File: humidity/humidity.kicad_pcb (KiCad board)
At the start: 2 copper layers, 59.7 x 27.9 mm, 19 parts, among them J1 Battery Holder, J2 Conn_01x06, U1 BME280, U2 ESP32-WROOM-32, U3 HT7333-A-SOT89

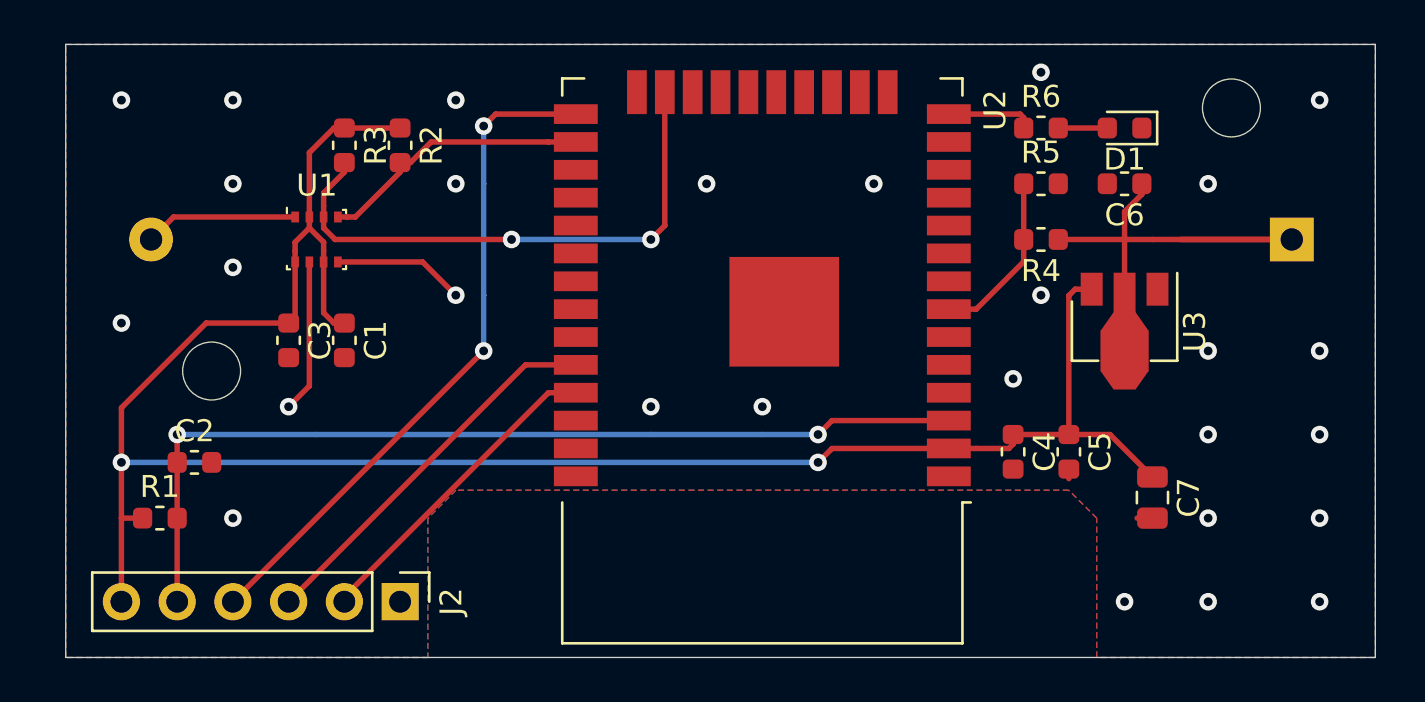
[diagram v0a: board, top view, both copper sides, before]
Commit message: Updates for Lifepo4 battery
Use a 3.2V lifepo4 battery.  This eliminates the need for a regulator.

Remove the battery sensing circuit - the esp32 ADC should be able to
sense VDD33 directly.

Add an N-MOSFET on BATT- to protect against battery reverse polarity.

Use 0805 LED size.  Adjust LED resistor to 100ohm.

Use wider traces for VBATT lines.
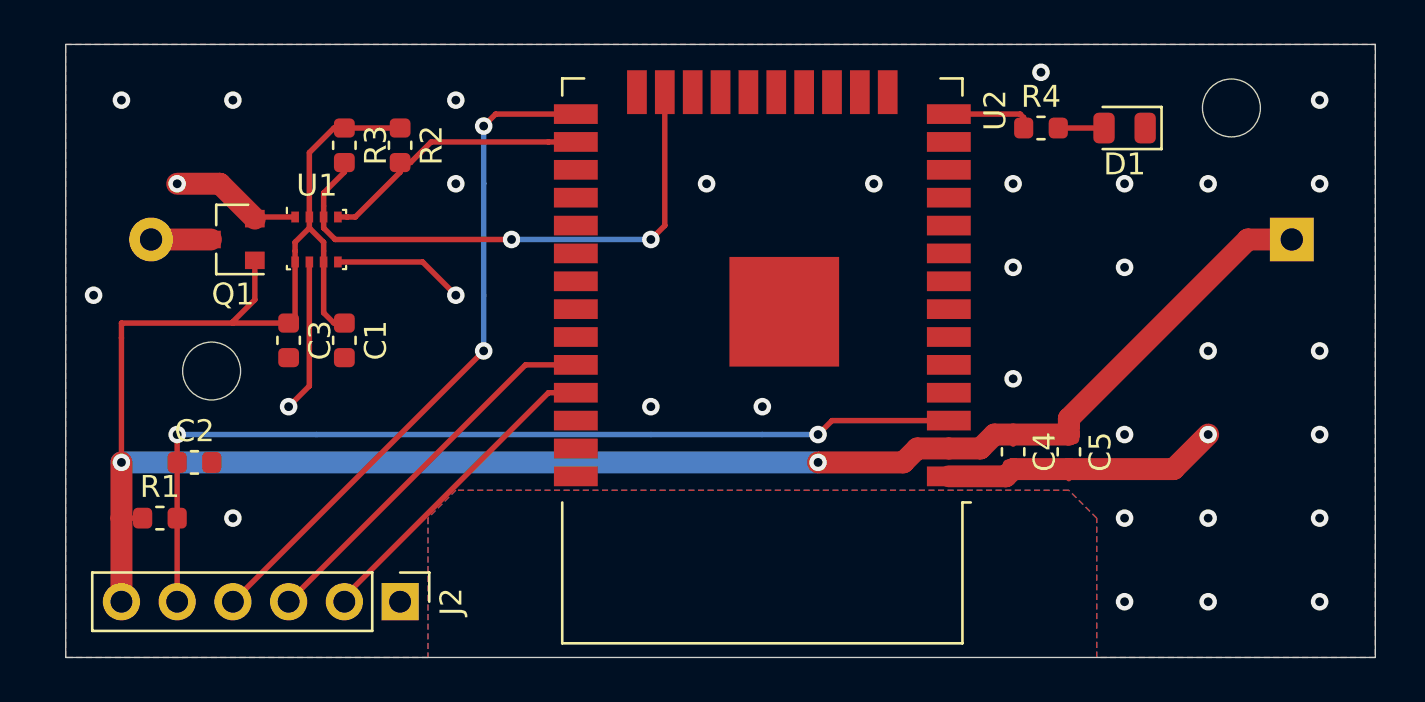
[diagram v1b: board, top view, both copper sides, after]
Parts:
- removed C6: 10uF, Capacitor_SMD:C_0603_1608Metric
- removed C7: 47uF, Capacitor_SMD:C_0805_2012Metric
- removed the R4 at (194.3, 116.8)
- removed R5: 1M, Resistor_SMD:R_0603_1608Metric
- removed U3: HT7333-A-SOT89, Package_TO_SOT_SMD:SOT-89-3
- added Q1: Q_NMOS_GSD, Package_TO_SOT_SMD:SOT-23, F.Cu at (157.5, 116.8)
- D1: footprint LED_SMD:LED_0603_1608Metric -> LED_SMD:LED_0805_2012Metric
- R4: renamed from R6; value 1K -> 0K1
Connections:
- C1 pad 1: +3V3 -> +BATT
- C3 pad 1: +3V3 -> +BATT
- C4 pad 1: +3V3 -> +BATT
- C5 pad 1: +3V3 -> +BATT
- J1 pad 2: GND -> Net-(J1-Pad2)
- J2 pad 6: +3V3 -> +BATT
- R1 pad 1: +3V3 -> +BATT
- R2 pad 1: +3V3 -> +BATT
- R3 pad 1: +3V3 -> +BATT
- U1 pad 2: +3V3 -> +BATT
- U1 pad 6: +3V3 -> +BATT
- U1 pad 8: +3V3 -> +BATT
- U2 pad 2: +3V3 -> +BATT
- U2 pad 7: VSENSE -> Net-(U2-Pad7)
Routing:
- net +3V3: track 93.1 -> 0.00 mm, vias 2 -> 0
- net +BATT: track 25.0 -> 101.0 mm, vias 0 -> 2
- net GND: track 21.1 -> 32.1 mm, vias 28 -> 33
- net VSENSE: track 7.86 -> 0.00 mm
- net Net-(J1-Pad2): track 0.00 -> 2.73 mm

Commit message: Updates for JLCPCB
Add LCSC part numbers (in case using JLCPCB to assemble).

Use 0805 for the caps (as they're cheaper on JLCPCB).

Add version information to silk screen.  Add a warning about
appropriate battery to the silk screen.
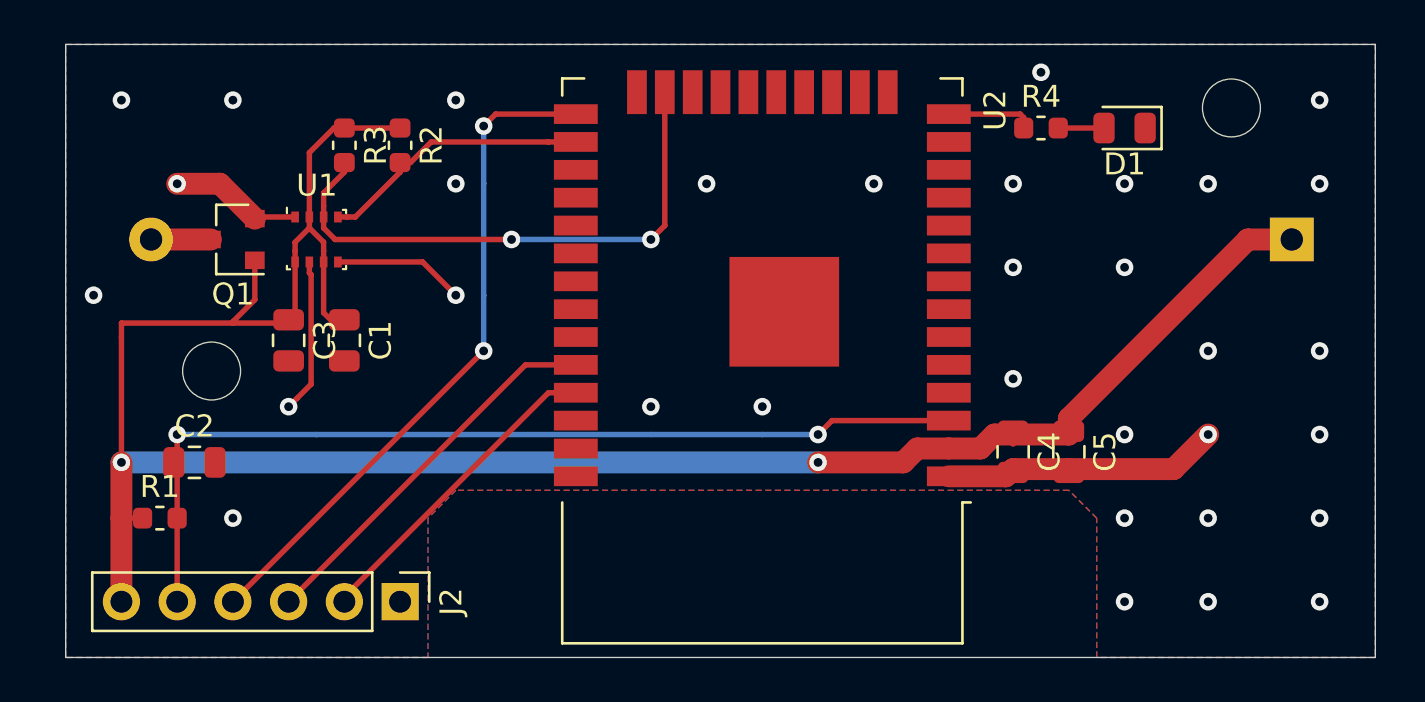
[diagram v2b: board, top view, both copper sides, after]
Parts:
- C1, C2, C3, C4, C5: footprint Capacitor_SMD:C_0603_1608Metric -> Capacitor_SMD:C_0805_2012Metric
- D1: value LED -> Red LED
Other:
- board text added: "3.2V Lifepo4 ONLY"
- board text added: "Humidity v0.3"

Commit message: Rework bme280 wire routing
Simplify the wiring to the bme280.  Improve the cap locations near the
bme280.

Add a 10K resistor to MOSFET gate (for ESD).

Fix location of silk screen text.
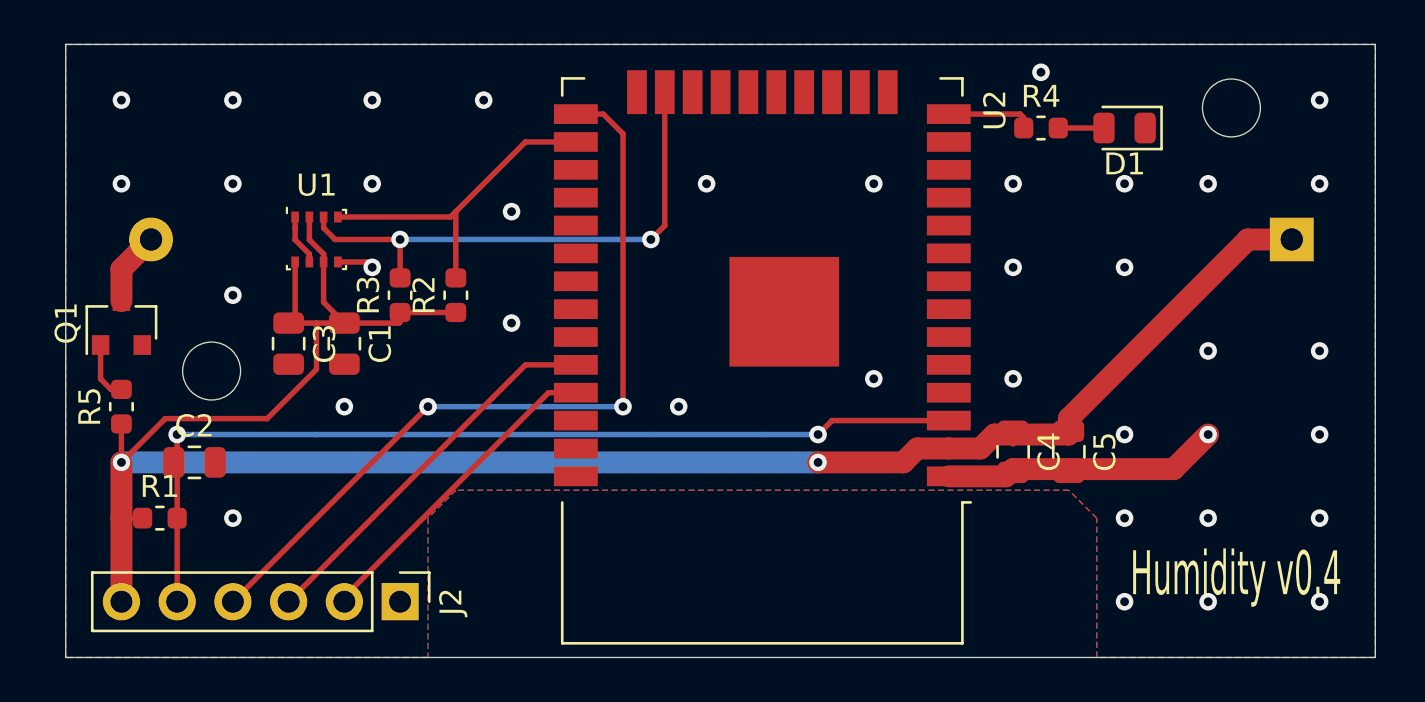
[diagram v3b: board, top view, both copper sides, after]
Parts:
- added R5: 10K, Resistor_SMD:R_0603_1608Metric, F.Cu at (152.4, 124.5)
- moved R2 7.29 mm to (167.6, 119.4), turned to 90 degrees
- moved R3 7.29 mm to (165.1, 119.4), turned to 90 degrees
- moved Q1 6.35 mm to (152.4, 120.7), turned to 90 degrees
- moved C1 0.15 mm to (162.6, 121.6)
- moved C3 0.15 mm to (160.0, 121.6)
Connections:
- Q1 pad 1: +BATT -> Net-(Q1-Pad1)
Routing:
- net GND: track 32.2 -> 17.0 mm, vias 33 -> 37
- net BOOT: track 30.8 -> 36.4 mm
- net +BATT: track 101.0 -> 96.7 mm
- net SCL: track 12.5 -> 15.3 mm
- net Net-(Q1-Pad1): track 0.00 -> 2.69 mm
- net SDA: track 25.8 -> 24.4 mm
- net Net-(J1-Pad2): track 2.73 -> 3.48 mm
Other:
- board text added: "Humidity v0.4"
- board text removed: "Humidity v0.3"

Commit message: Further updates to n-mosfet
Use AO3416 n-mosfet (which has ESD).

Move n-mosfet to corner.  Relocate the n-mosfet away from the edge and
to reduce crowding.

Minor wire routing improvements.
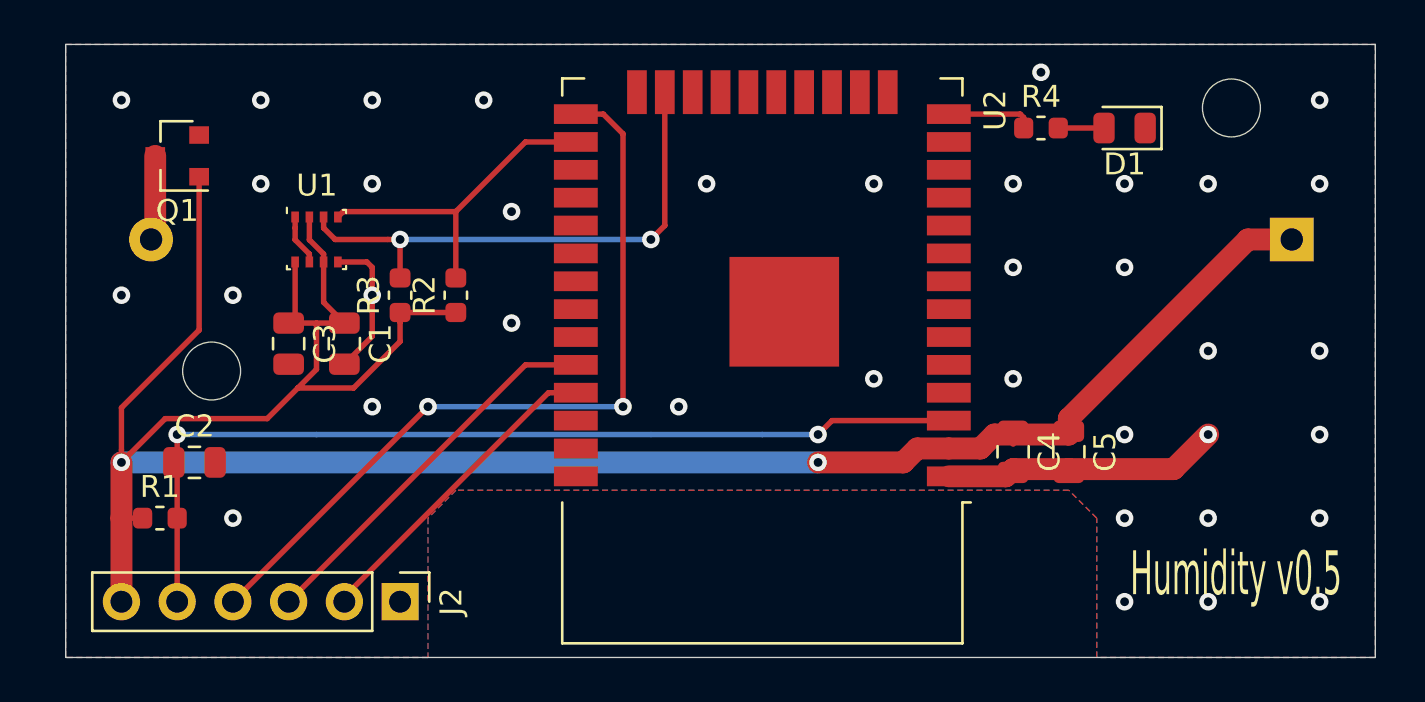
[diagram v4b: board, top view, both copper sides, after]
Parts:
- removed R5: 10K, Resistor_SMD:R_0603_1608Metric
- moved Q1 8.03 mm to (154.9, 113.0), turned to 180 degrees
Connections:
- Q1 pad 1: Net-(Q1-Pad1) -> +BATT
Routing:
- net +BATT: track 96.7 -> 114.3 mm
- net GND: track 17.0 -> 22.0 mm
- net Net-(Q1-Pad1): track 2.69 -> 0.00 mm
- net Net-(J1-Pad2): track 3.48 -> 4.00 mm
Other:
- board text added: "Humidity v0.5"
- board text removed: "Humidity v0.4"
